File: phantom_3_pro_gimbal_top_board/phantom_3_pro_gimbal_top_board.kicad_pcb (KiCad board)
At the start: 2 copper layers, 67.2 x 57.3 mm, 578 parts

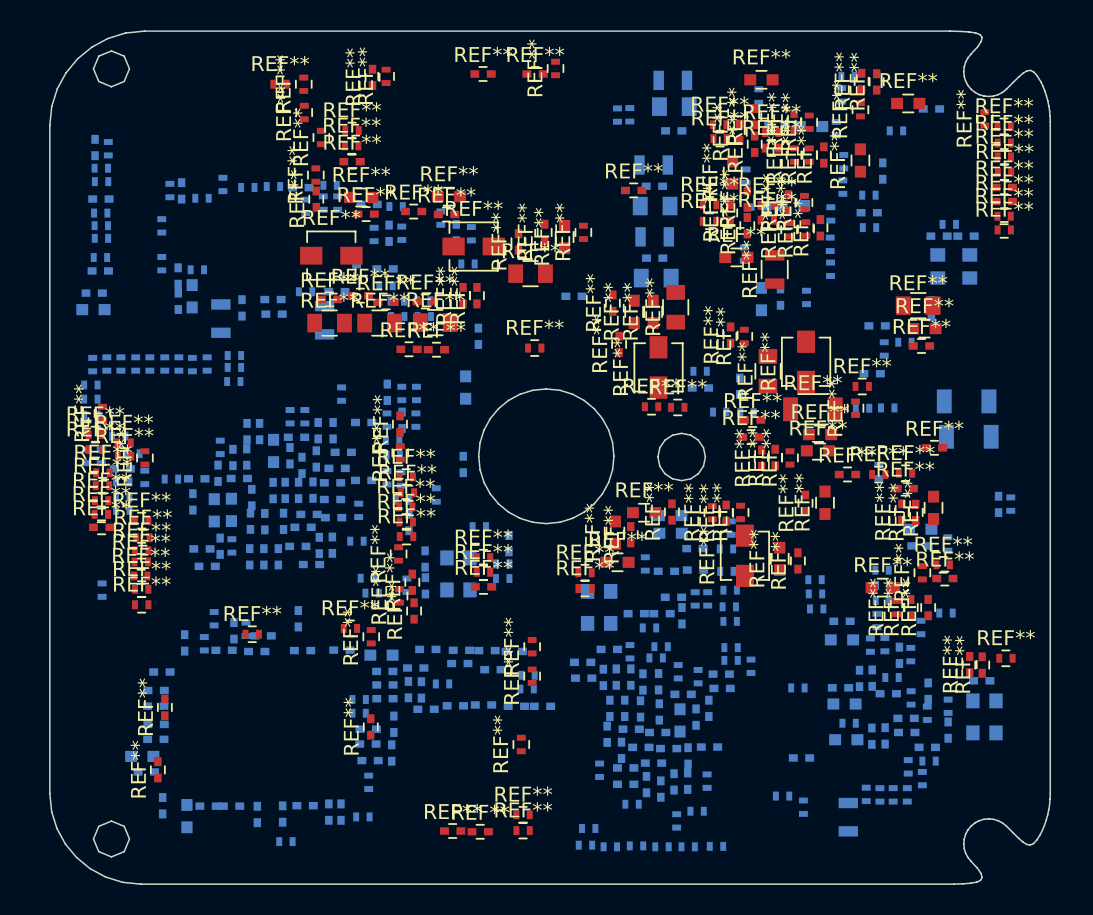
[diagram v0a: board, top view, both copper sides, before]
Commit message: Gimbal Top: Better symbols, dc-dc circuits
Symbols were updated so that pins match to footpints.
More footprints added.
Switching regulator circuits were drawn based on application examples.
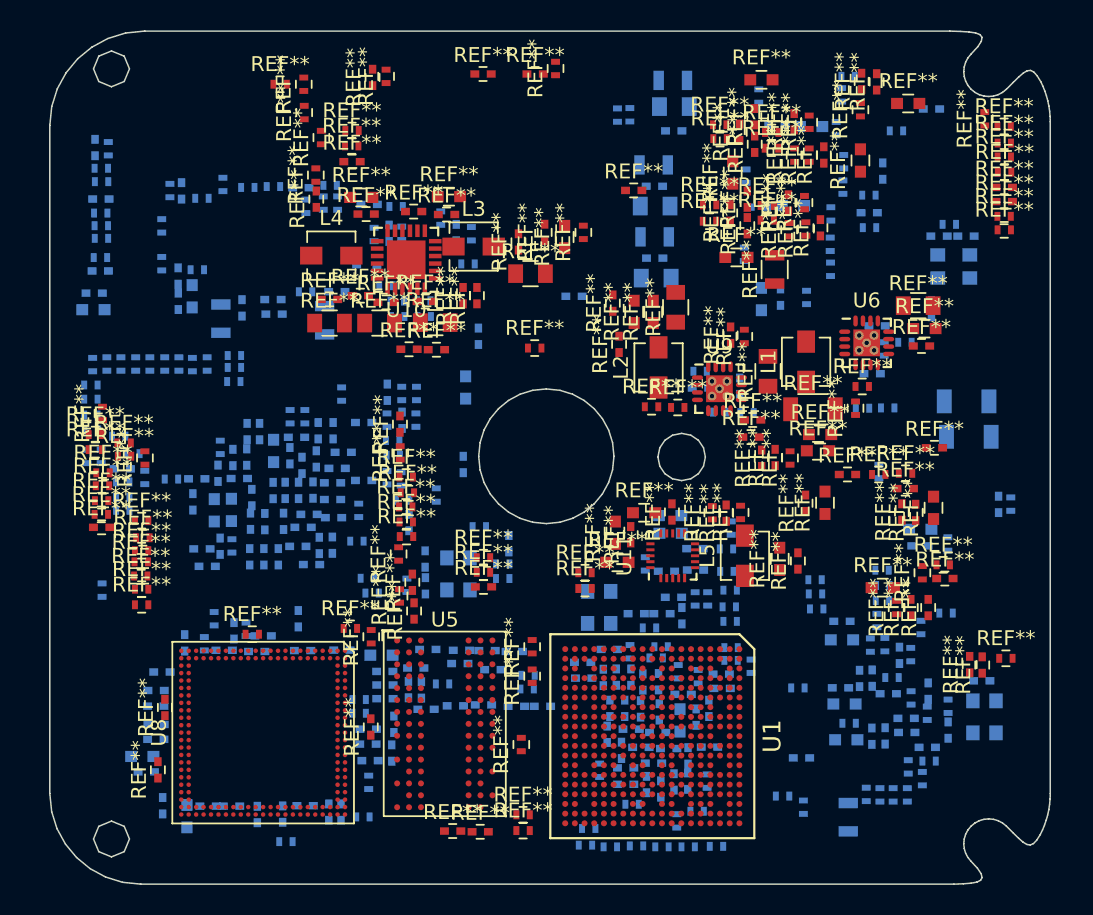
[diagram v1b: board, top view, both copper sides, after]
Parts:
- added U1: TMS320DM365_ZCE_338, Housings_BGA-v2:PBGA-N338_19x19_13x13mm_Pitch0.65mm, F.Cu at (53.2, 60.1)
- added U10: LM26480-Q1_WQFN_24, Housings_DFN_QFN:QFN-24-1EP_4x4mm_Pitch0.5mm, F.Cu at (36.7, 28.1)
- added U11: TPS650061_RUK_20, Housings_DFN_QFN-v2:QFN-20_3x3mm_Pitch0.4mm_NoMask, F.Cu at (54.6, 48.0)
- added U5: IS43DR16640B, Housings_BGA-v2:BGA-84_2x3x15_8.0x12.5mm_Pitch0.8mm, F.Cu at (39.3, 59.7)
- added U6: TLV62130, Housings_DFN_QFN:QFN-16-1EP_3x3mm_Pitch0.5mm_ThermalVias, F.Cu at (67.6, 33.7)
- added U8: EDB8132B3PB_DDR2_RAM, Housings_BGA-v2:UFBGA-168_12x12mm_Pitch0.5mm, F.Cu at (27.1, 59.9)
- added U9: TLV62130, Housings_DFN_QFN:QFN-16-1EP_3x3mm_Pitch0.5mm_ThermalVias, F.Cu at (57.7, 36.8)
- L1, L2, L3, L4, L5: renamed from REF**; value L_Vishay_IHLP-1212 -> 2.2uH
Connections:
- L1 pad 1: (no net) -> Net-(L1-Pad1)
- L1 pad 2: (no net) -> Net-(C4-Pad1)
- L2 pad 1: (no net) -> Net-(L2-Pad1)
- L2 pad 2: (no net) -> Net-(C8-Pad1)
- L3 pad 1: (no net) -> Net-(L3-Pad1)
- L3 pad 2: (no net) -> Net-(C11-Pad1)
- L4 pad 1: (no net) -> Net-(L4-Pad1)
- L4 pad 2: (no net) -> Net-(C18-Pad1)
- L5 pad 1: (no net) -> Net-(L5-Pad1)
- L5 pad 2: (no net) -> /VOUT_1.2

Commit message: Gimbal Top: Measured and filled part of DC-DC conv
Checked part of voltage regulator circuits with multimeter.
Associated a few footprints with schematic, updated values.
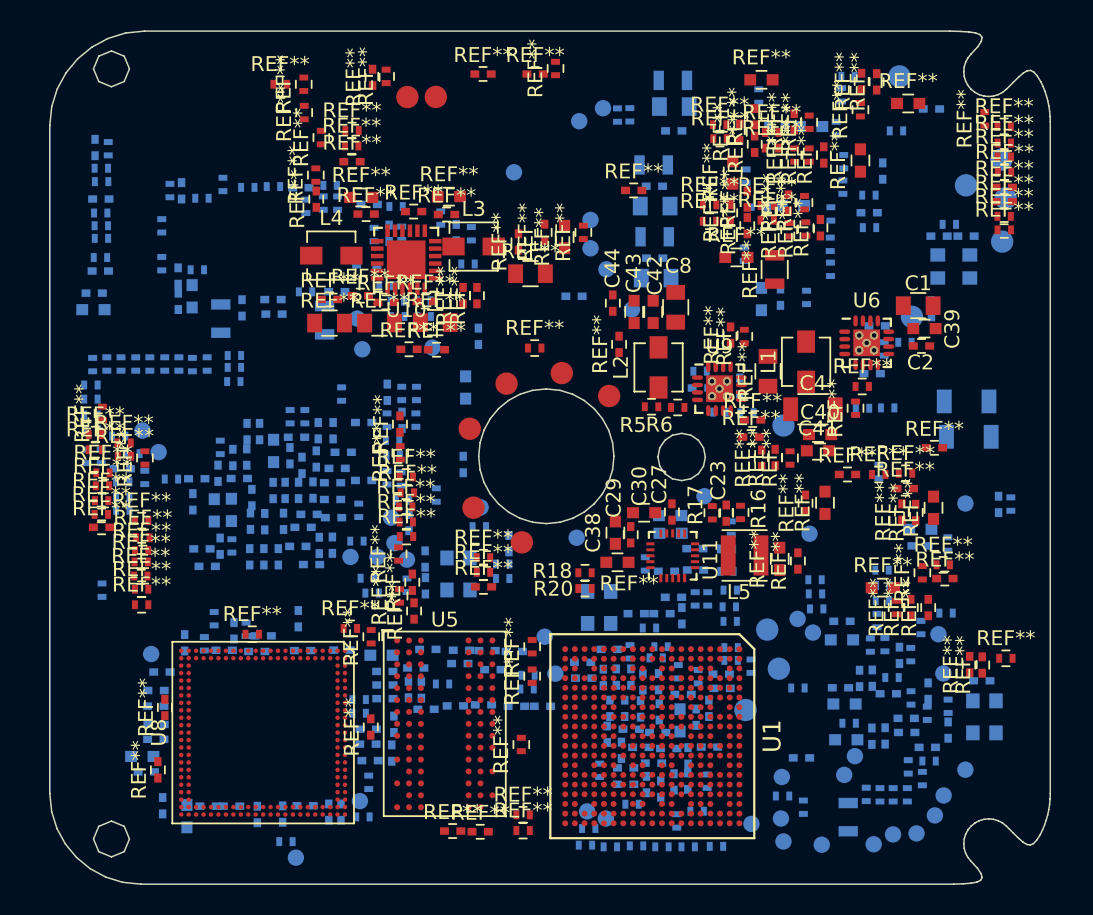
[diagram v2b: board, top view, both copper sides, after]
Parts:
- added TP1: CS_DSP, Measurement_Points:Measurement_Point_Round-SMD-Pad_Small, B.Cu at (61.9, 62.9)
- added TP10: TDI, Measurement_Points:Measurement_Point_Round-SMD-Pad_Small, B.Cu at (36.7, 48.3)
- added TP11: PGED, Measurement_Points:Measurement_Point_Round-SMD-Pad_Small, B.Cu at (76.7, 21.4)
- added TP12: PGEC, Measurement_Points:Measurement_Point_Round-SMD-Pad_Small, B.Cu at (74.3, 23.1)
- added TP13: SWCLK, Measurement_Points:Measurement_Point_Round-SMD-Pad_Small, B.Cu at (59.9, 66.0)
- added TP14: TDO, Measurement_Points:Measurement_Point_Round-SMD-Pad_Small, B.Cu at (33.0, 48.1)
- added TP15: MCLR_N, Measurement_Points:Measurement_Point_Round-SMD-Pad_Small, B.Cu at (69.8, 15.8)
- added TP16: BOOT0, Measurement_Points:Measurement_Point_Round-SMD-Pad_Small, B.Cu at (74.2, 62.4)
- added TP17: MOSI, Measurement_Points:Measurement_Point_Round-SMD-Pad_Small, B.Cu at (62.0, 67.2)
- added TP18: SWDIO, Measurement_Points:Measurement_Point_Round-SMD-Pad_Small, B.Cu at (61.9, 65.7)
- added TP19: RST, Measurement_Points:Measurement_Point_Round-SMD-Pad_Small, B.Cu at (35.7, 45.5)
- added TP2: SCL_DSP, Measurement_Points:Measurement_Point_Round-SMD-Pad_Small, B.Cu at (64.6, 67.4)
- added TP20: RSTEX, Measurement_Points:Measurement_Point_Round-SMD-Pad_Small, B.Cu at (41.7, 44.8)
- added TP21: BT01, Measurement_Points:Measurement_Point_Round-SMD-Pad_Small, B.Cu at (50.1, 65.7)
- added TP22: BT00, Measurement_Points:Measurement_Point_Round-SMD-Pad_Small, B.Cu at (48.8, 65.2)
- added TP23: MC, Measurement_Points:Measurement_Point_Round-SMD-Pad_Small, B.Cu at (43.9, 22.2)
- added TP24: B_S, Measurement_Points:Measurement_Point_Round-SMD-Pad_Small, B.Cu at (66.1, 62.7)
- added TP25: 365, Measurement_Points:Measurement_Point_Round-SMD-Pad_Small, B.Cu at (33.6, 64.5)
- added TP26: OUT6, Measurement_Points:Measurement_Point_Round-SMD-Pad_Small, B.Cu at (20.1, 41.0)
- added TP27: OUT8, Measurement_Points:Measurement_Point_Round-SMD-Pad_Small, B.Cu at (19.0, 39.6)
- added TP28: GIMBAL, Measurement_Points:Measurement_Point_Round-SMD-Pad_Small, B.Cu at (29.3, 68.3)
- added TP29: CLK, Measurement_Points:Measurement_Point_Round-SMD-Pad_Small, B.Cu at (35.9, 47.2)
- added TP3: U0_R, Measurement_Points:Measurement_Point_Round-SMD-Pad_Small, F.Cu at (41.0, 39.5)
- added TP30: U1_T1, Measurement_Points:Measurement_Point_Round-SMD-Pad_Small, B.Cu at (72.4, 53.3)
- added TP31: U1_R1, Measurement_Points:Measurement_Point_Round-SMD-Pad_Small, B.Cu at (72.8, 55.9)
- added TP32: 12V, Measurement_Points:Measurement_Point_Round-SMD-Pad_Small, B.Cu at (70.7, 32.0)
- added TP33: +5V, Measurement_Points:Measurement_Point_Round-SMD-Pad_Small, B.Cu at (62.0, 39.3)
- added TP34: CANH, Measurement_Points:Measurement_Point_Round-SMD-Pad_Small, B.Cu at (71.0, 66.7)
- added TP35: CANL, Measurement_Points:Measurement_Point_Round-SMD-Pad_Small, B.Cu at (68.1, 67.4)
- added TP36: 3.3VD, Measurement_Points:Measurement_Point_Round-SMD-Pad_Small, B.Cu at (76.7, 26.9)
- added TP37: A9S_3.3VD, Measurement_Points:Measurement_Point_Round-SMD-Pad_Small, B.Cu at (38.5, 34.0)
- added TP38: ﻿3V3VD, Measurement_Points:Measurement_Point_Round-SMD-Pad_Small, F.Cu at (38.7, 17.2)
- added TP39: 3.3VD, Measurement_Points:Measurement_Point_Round-SMD-Pad_Small, B.Cu at (74.2, 44.5)
- added TP4: U0_T, Measurement_Points:Measurement_Point_Round-SMD-Pad_Small, F.Cu at (41.2, 44.8)
- added TP40: VCC3V3, Measurement_Points:Measurement_Point_Round-SMD-Pad_Small, B.Cu at (56.7, 44.0)
- added TP41: 1.8VD, Measurement_Points:Measurement_Point_Round-SMD-Pad_Small, B.Cu at (33.7, 34.1)
- added TP42: VCC1V8, Measurement_Points:Measurement_Point_Round-SMD-Pad_Small, B.Cu at (48.1, 46.8)
- added TP43: MB, Measurement_Points:Measurement_Point_Round-SMD-Pad_Small, B.Cu at (48.3, 18.8)
- added TP44: MA, Measurement_Points:Measurement_Point_Round-SMD-Pad_Small, B.Cu at (49.9, 17.9)
- added TP45: H2, Measurement_Points:Measurement_Point_Round-SMD-Pad_Small, B.Cu at (49.1, 25.4)
- added TP46: H1, Measurement_Points:Measurement_Point_Round-SMD-Pad_Small, B.Cu at (49.1, 27.4)
- added TP47: H3, Measurement_Points:Measurement_Point_Round-SMD-Pad_Small, B.Cu at (50.1, 28.8)
- added TP48: U1RT, Measurement_Points:Measurement_Point_Round-SMD-Pad_Small, B.Cu at (72.2, 65.5)
- added TP49: U1TT, Measurement_Points:Measurement_Point_Round-SMD-Pad_Small, B.Cu at (69.4, 66.7)
- added TP5: U3_CX, Measurement_Points:Measurement_Point_Round-SMD-Pad_Small, B.Cu at (46.7, 55.9)
- added TP50: URAT2_TX, Measurement_Points:Measurement_Point_Round-SMD-Pad_Small, F.Cu at (47.1, 35.7)
- added TP51: URAT2_RX, Measurement_Points:Measurement_Point_Round-SMD-Pad_Small, F.Cu at (43.4, 36.5)
- added TP52: VDDA, Measurement_Points:Measurement_Point_Round-SMD-Pad_Small, B.Cu at (33.4, 32.1)
- added TP53: VDD, Measurement_Points:Measurement_Point_Round-SMD-Pad_Small, B.Cu at (51.9, 31.5)
- added TP54: 1V2, Measurement_Points:Measurement_Point_Round-SMD-Pad_Small, B.Cu at (63.8, 46.5)
- added TP55: 1.25DDR2, Measurement_Points:Measurement_Point_Round-SMD-Pad_Small, B.Cu at (19.6, 54.6)
- added TP56: GND, Measurement_Points:Measurement_Point_Round-SMD-Pad_Small, F.Cu at (36.8, 17.2)
- added TP57: GND, Measurement_Points:Measurement_Point_Round-SMD-Pad_Small, B.Cu at (72.8, 64.1)
- added TP58: GND, Measurement_Points:Measurement_Point_Round-SMD-Pad_Small, F.Cu at (44.5, 47.1)
- added TP59: GND, Measurement_Points:Measurement_Point_Round-SMD-Pad_Small, F.Cu at (50.3, 37.3)
- added TP6: U3_RX, Measurement_Points:Measurement_Point_Round-SMD-Pad_Small, B.Cu at (46.0, 53.5)
- added TP60: GND, Measurement_Points:Measurement_Point_Round-SMD-Pad_Small, B.Cu at (59.5, 58.4)
- added TP61: GND, Measurement_Points:Measurement_Point_Round-SMD-Pad_Small, B.Cu at (66.8, 61.5)
- added TP62: GND, Measurement_Points:Measurement_Point_Round-SMD-Pad_Small, B.Cu at (77.0, 24.0)
- added TP63: 368_U0_RXP, Measurement_Points:Measurement_Point_Round-SMD-Pad_Small, B.Cu at (61.7, 55.6)
- added TP64: 368_U0_TXP, Measurement_Points:Measurement_Point_Round-SMD-Pad_Small, B.Cu at (60.9, 53.0)
- added TP7: DM-, Measurement_Points:Measurement_Point_Round-SMD-Pad_Small, B.Cu at (63.0, 52.2)
- added TP8: DP+, Measurement_Points:Measurement_Point_Round-SMD-Pad_Small, B.Cu at (64.0, 53.2)
- added TP9: TMS, Measurement_Points:Measurement_Point_Round-SMD-Pad_Small, B.Cu at (34.8, 48.1)
- L5: value 2.2uH -> L_Neosid_SMS-ME3010; footprint Inductors_SMD:L_Vishay_IHLP-1212 -> Inductors_SMD:L_Neosid_SMS-ME3010
- U1: value TMS320DM365_ZCE_338 -> TMS320DM365
- U10: value LM26480-Q1_WQFN_24 -> LM26480
- U11: value TPS650061_RUK_20 -> TPS650061
- U8: value EDB8132B3PB_DDR2_RAM -> EDB8132B3PB
- turned L5 to 0 degrees
- renumbered REF** to C1, REF** to C2, REF** to C23, REF** to C27, REF** to C29, REF** to C30, REF** to C34, REF** to C35, REF** to C36, REF** to C37, REF** to C38, REF** to C39, REF** to C4, REF** to C40, REF** to C41, REF** to C42, REF** to C43, REF** to C44, REF** to C8, REF** to R16, REF** to R17, REF** to R18, REF** to R20, REF** to R27, REF** to R5, REF** to R6
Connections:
- L5 pad 1: Net-(L5-Pad1) -> (no net)
- L5 pad 2: /VOUT_1.2 -> (no net)

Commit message: Gimbal Top: Added more symbols and footprints.
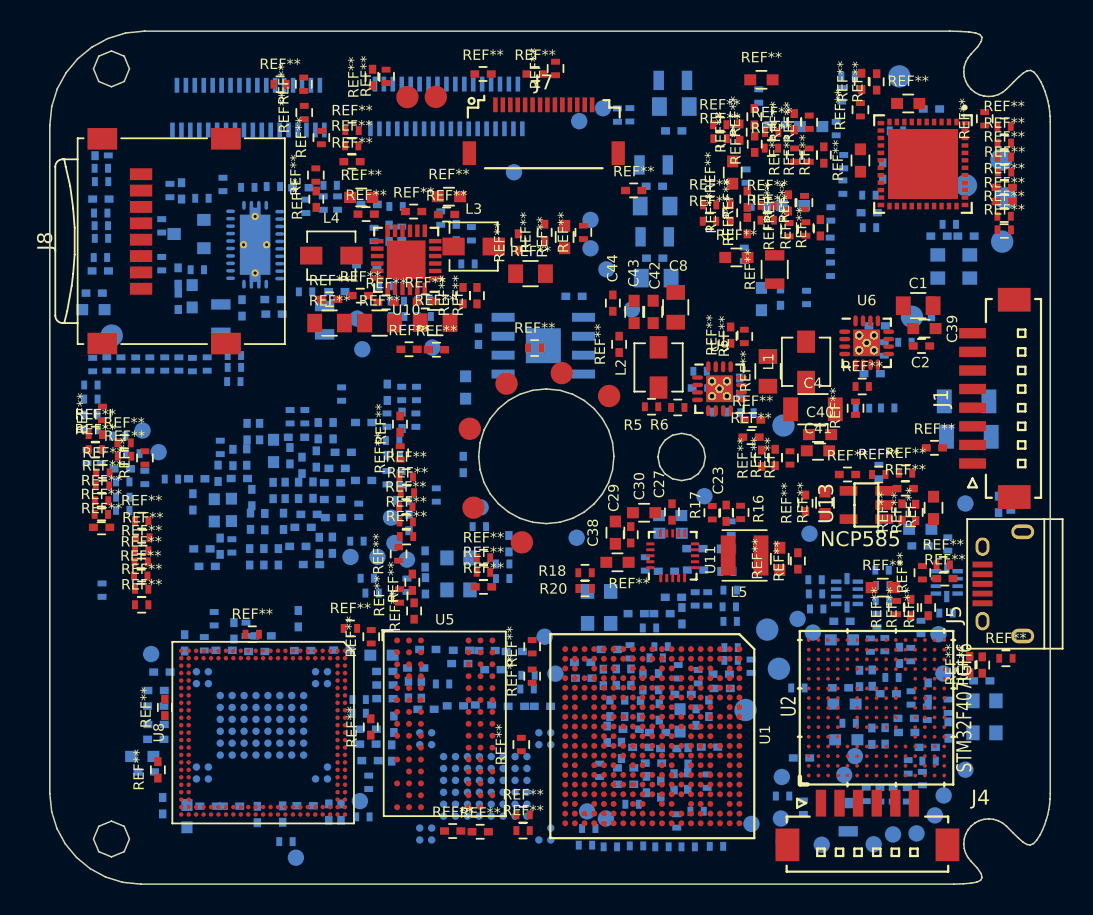
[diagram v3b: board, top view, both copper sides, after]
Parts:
- added J1: CONN_CENTER, Connectors_Hirose:Hirose_DF13C-08P-1.25V_08x1.25mm_Straight, F.Cu at (76.1, 37.4)
- added J2: CONN_ARMS2, Connectors_FFC:Flat_Foam_Conn-ZIF-35D-0.6H_35x0.60mm_Angled, B.Cu at (39.4, 17.8)
- added J3: CONN_ARMS1, Connectors_FFC:Flat_Foam_Conn-ZIF-35D-0.6H_35x0.60mm_Angled, B.Cu at (26.1, 17.9)
- added J4: CONN_OFDM, Connectors_Hirose:Hirose_DF13C-06P-1.25V_06x1.25mm_Straight, F.Cu at (67.7, 66.0)
- added J5: USB_OTG, Connectors:USB_Micro-B, F.Cu at (76.8, 49.9)
- added J7: CONN_MOTOR, Connectors_FFC:Flat_Foam_Conn-14S-0.5H_14x0.50mm_Angled, F.Cu at (45.9, 19.7)
- added J8: Micro_SD_Card, Connectors:microSD_Card_Receptacle_Wuerth_693072010801, F.Cu at (21.6, 26.9)
- added Q1: PMBT3904, TO_SOT_Packages_SMD:SOT-23, B.Cu at (22.1, 26.4)
- added TP65: GND, Measurement_Points:Measurement_Point_Round-SMD-Pad_Small, B.Cu at (16.9, 33.2)
- added U12: MLX90316, Housings_SOIC:SOIC-8-1EP_3.9x4.9mm_Pitch1.27mm, B.Cu at (45.9, 33.9)
- added U13: NCP585, TO_SOT_Packages_SMD-v2:SOT-25, F.Cu at (67.6, 44.6)
- added U14: TS3USB221A-Q1, texas-var-geda:RSE10, B.Cu at (73.0, 49.8)
- added U15: TS3USB221A-Q1, texas-var-geda:RSE10, B.Cu at (66.3, 50.5)
- added U16: dsPIC33EP128MC504, Housings_LGA-v2:VTLA-44_LGA-44_6x6mm_Pitch0.5mm, F.Cu at (71.4, 21.7)
- added U2: STM32F407IGH6, Housings_BGA-v2:UFBGA176p25-10x10mm_pitch0.65mm, F.Cu at (68.3, 58.2)
- added U3: MT29F1G08, Housings_BGA-v2:VFBGA-63_11x9_9.0x7.4mm_Pitch0.8mm, B.Cu at (42.0, 63.5)
- added U4: MT29F2G08, Housings_BGA-v2:VFBGA-63_11x9_9.0x7.4mm_Pitch0.8mm, B.Cu at (27.0, 59.4)
- added U7: SN74AVC8T245RHL, Housings_DFN_QFN-v2:RHL0024_PVQFN-n24p4_4.3x6.3mm_Pitch0.5mm, B.Cu at (26.5, 27.1)
- C1: value C_0805 -> 10uF?
- C2: value C_0402 -> 100nF?
- C23: value C_0402 -> 22pF
- C27, C29: value C_0402 -> 10nF?
- C30, C37, C38: value C_0603 -> 2.2uF?
- C34: value C_0402 -> 1uF?
- C35, C36: value C_1206 -> 22uF?
- C39, C40, C42: value C_0603 -> 100nF?
- C4: value C_1206 -> 2.2uF?
- C41, C43: value C_0603 -> 10nF?
- C44: value C_0402 -> 100pF?
- C8: value C_0805 -> 2.2uF?
- L5: value L_Neosid_SMS-ME3010 -> 2.2uH
- R16, R17: value R_0402 -> 220kΩ
- R18: value R_0402 -> 1kΩ
- R20: value R_0402 -> 50kΩ
- R27: value R_0402 -> 2kΩ
- R5, R6: value R_0402 -> 2.8kΩ?
- REF**: value R_0805 -> (none)
- TP38: value ﻿3V3VD -> 3V3VD
- U1: value TMS320DM365 -> TMS320DM365ZCE
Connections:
- net Net-(TP52-Pad1) renamed /VDDA1V1
- C1 pad 1: (no net) -> PVIN
- C1 pad 2: (no net) -> GND
- C2 pad 1: (no net) -> PVIN
- C2 pad 2: (no net) -> GND
- C23 pad 1: (no net) -> /VCC1V2
- C23 pad 2: (no net) -> Net-(C23-Pad2)
- C27 pad 1: (no net) -> /VCC3V3
- C27 pad 2: (no net) -> GND
- C29 pad 1: (no net) -> /VCC1V8
- C29 pad 2: (no net) -> GND
- C30 pad 1: (no net) -> PVIN
- C30 pad 2: (no net) -> GND
- C34 pad 1: (no net) -> /EN_3.3
- C34 pad 2: (no net) -> GND
- C35 pad 1: (no net) -> PVIN
- C35 pad 2: (no net) -> GND
- C36 pad 1: (no net) -> PVIN
- C36 pad 2: (no net) -> GND
- C37 pad 1: (no net) -> /VCC3V3
- C37 pad 2: (no net) -> GND
- C38 pad 1: (no net) -> /VCC1V8
- C38 pad 2: (no net) -> GND
- C39 pad 1: (no net) -> PVIN
- C39 pad 2: (no net) -> GND
- C4 pad 1: (no net) -> PVIN
- C4 pad 2: (no net) -> GND
- C40 pad 1: (no net) -> PVIN
- C40 pad 2: (no net) -> GND
- C41 pad 1: (no net) -> PVIN
- C41 pad 2: (no net) -> GND
- C42 pad 1: (no net) -> /VDD1V1
- C42 pad 2: (no net) -> GND
- C43 pad 1: (no net) -> /VDD1V1
- C43 pad 2: (no net) -> GND
- C44 pad 1: (no net) -> /VDD1V1
- C44 pad 2: (no net) -> GND
- C8 pad 1: (no net) -> /VDD1V1
- C8 pad 2: (no net) -> GND
- L1 pad 2: Net-(C4-Pad1) -> PVIN
- L2 pad 2: Net-(C8-Pad1) -> /VDD1V1
- L5 pad 1: (no net) -> Net-(L5-Pad1)
- L5 pad 2: (no net) -> /VCC1V2
- R16 pad 1: (no net) -> /VCC1V2
- R16 pad 2: (no net) -> Net-(C23-Pad2)
- R17 pad 1: (no net) -> Net-(C23-Pad2)
- R17 pad 2: (no net) -> GND
- R18 pad 1: (no net) -> /VCC3V3
- R18 pad 2: (no net) -> Net-(C26-Pad1)
- R20 pad 1: (no net) -> /VCC3V3
- R20 pad 2: (no net) -> Net-(R20-Pad2)
- R27 pad 1: (no net) -> /VCC1V8
- R27 pad 2: (no net) -> /EN_3.3
- R5 pad 1: (no net) -> /VDD1V1
- R5 pad 2: (no net) -> Net-(R5-Pad2)
- R6 pad 1: (no net) -> Net-(R5-Pad2)
- R6 pad 2: (no net) -> GND
- REF** pad 1: (no net) -> Net-(J4-Pad1)
- REF** pad 2: (no net) -> Net-(J4-Pad2)
- TP32 pad 1: Net-(TP32-Pad1) -> PVIN
- TP33 pad 1: Net-(TP33-Pad1) -> PVIN
- TP40 pad 1: Net-(TP40-Pad1) -> /VCC3V3
- TP42 pad 1: Net-(TP42-Pad1) -> /VCC1V8
- TP53 pad 1: Net-(TP53-Pad1) -> /VDD1V1
- TP54 pad 1: Net-(TP54-Pad1) -> /VCC1V2
- U1 pad E12: /VOUT_1.2 -> /VCC1V2
- U1 pad E5: /VOUT_1.8 -> /VCC1V8
- U1 pad E9: /VOUT_1.8 -> /VCC1V8
- U1 pad F6: /VOUT_3.3 -> /VCC3V3
- U1 pad F7: /VOUT_3.3 -> /VCC3V3
- U1 pad G6: /VOUT_1.2 -> /VCC1V2
- U1 pad G8: /VOUT_1.2 -> /VCC1V2
- U1 pad G9: /VOUT_1.8 -> /VCC1V8
- U1 pad H12: /VOUT_1.2 -> /VCC1V2
- U1 pad H6: /VOUT_3.3 -> /VCC3V3
- U1 pad H7: /VOUT_1.2 -> /VCC1V2
- U1 pad H8: /VOUT_1.2 -> /VCC1V2
- U1 pad J12: /VOUT_1.2 -> /VCC1V2
- U1 pad J14: /VOUT_1.2 -> /VCC1V2
- U1 pad J6: /VOUT_1.2 -> /VCC1V2
- U1 pad J7: /VOUT_1.8 -> /VCC1V8
- U1 pad J8: /VOUT_1.2 -> /VCC1V2
- U1 pad K12: /VOUT_1.2 -> /VCC1V2
- U1 pad K6: /VOUT_1.8 -> /VCC1V8
- U1 pad K7: /VOUT_1.2 -> /VCC1V2
- U1 pad K8: /VOUT_1.2 -> /VCC1V2
- U1 pad M5: /VOUT_1.2 -> /VCC1V2
- U1 pad N6: /VOUT_3.3 -> /VCC3V3
- U1 pad N9: /VOUT_1.8 -> /VCC1V8
- U1 pad P4: /VOUT_3.3 -> /VCC3V3
- U1 pad P5: /VOUT_3.3 -> /VCC3V3
- U1 pad P6: /VOUT_3.3 -> /VCC3V3
- U1 pad P7: /VOUT_1.8 -> /VCC1V8
- U1 pad P9: /VOUT_1.8 -> /VCC1V8
- U11 pad 13: /VOUT_3.3 -> /VCC3V3
- U11 pad 14: /VOUT_3.3 -> /VCC3V3
- U11 pad 15: /VIN -> PVIN
- U11 pad 16: /VOUT_1.8 -> /VCC1V8
- U11 pad 17: /VOUT_1.8 -> /VCC1V8
- U11 pad 18: /VIN -> PVIN
- U11 pad 8: /VIN -> PVIN
- U11 pad 9: /VIN -> PVIN
- U6 pad 14: Net-(C4-Pad1) -> PVIN
- U9 pad 14: Net-(C8-Pad1) -> /VDD1V1
